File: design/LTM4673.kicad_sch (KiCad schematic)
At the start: 96 parts, among them U35 LTM4673IY#PBF

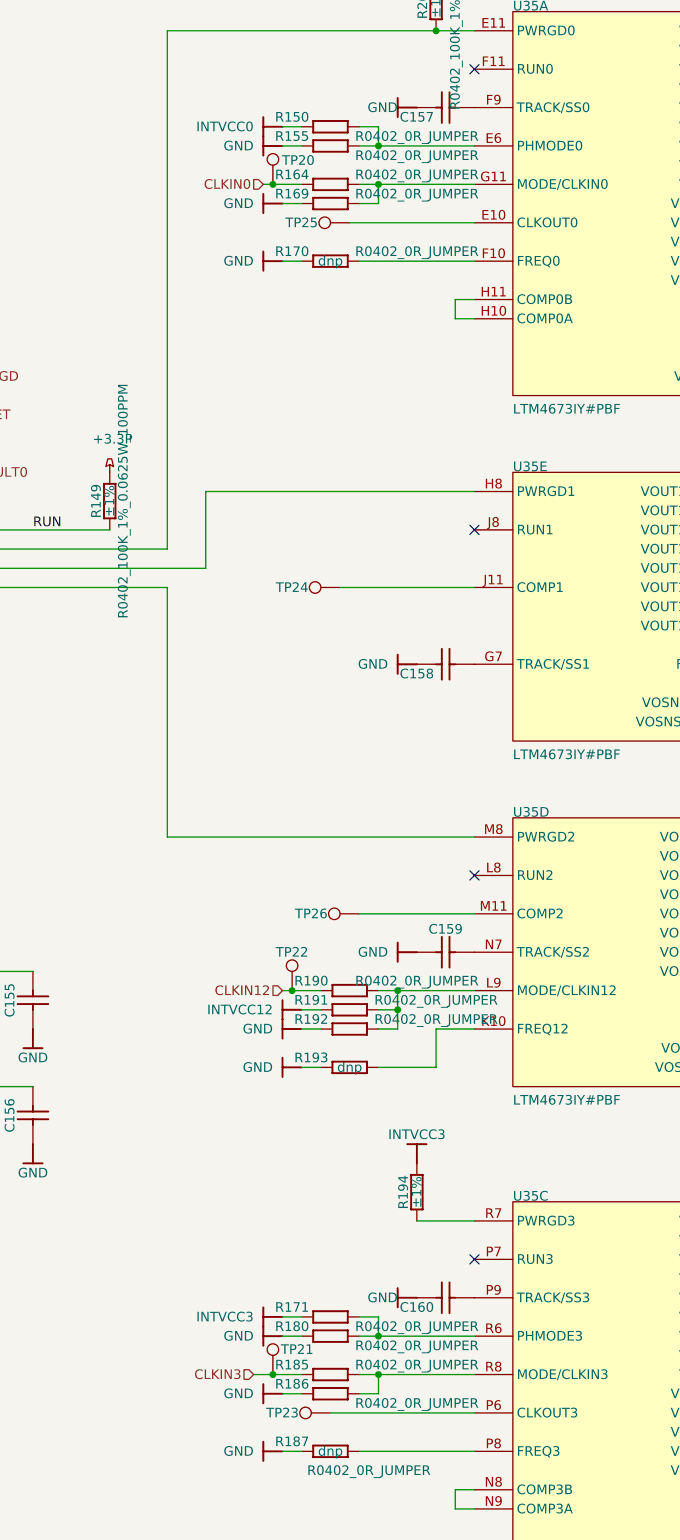
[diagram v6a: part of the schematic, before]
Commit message: some resistors marked as DNP
some resistors marked as DNP
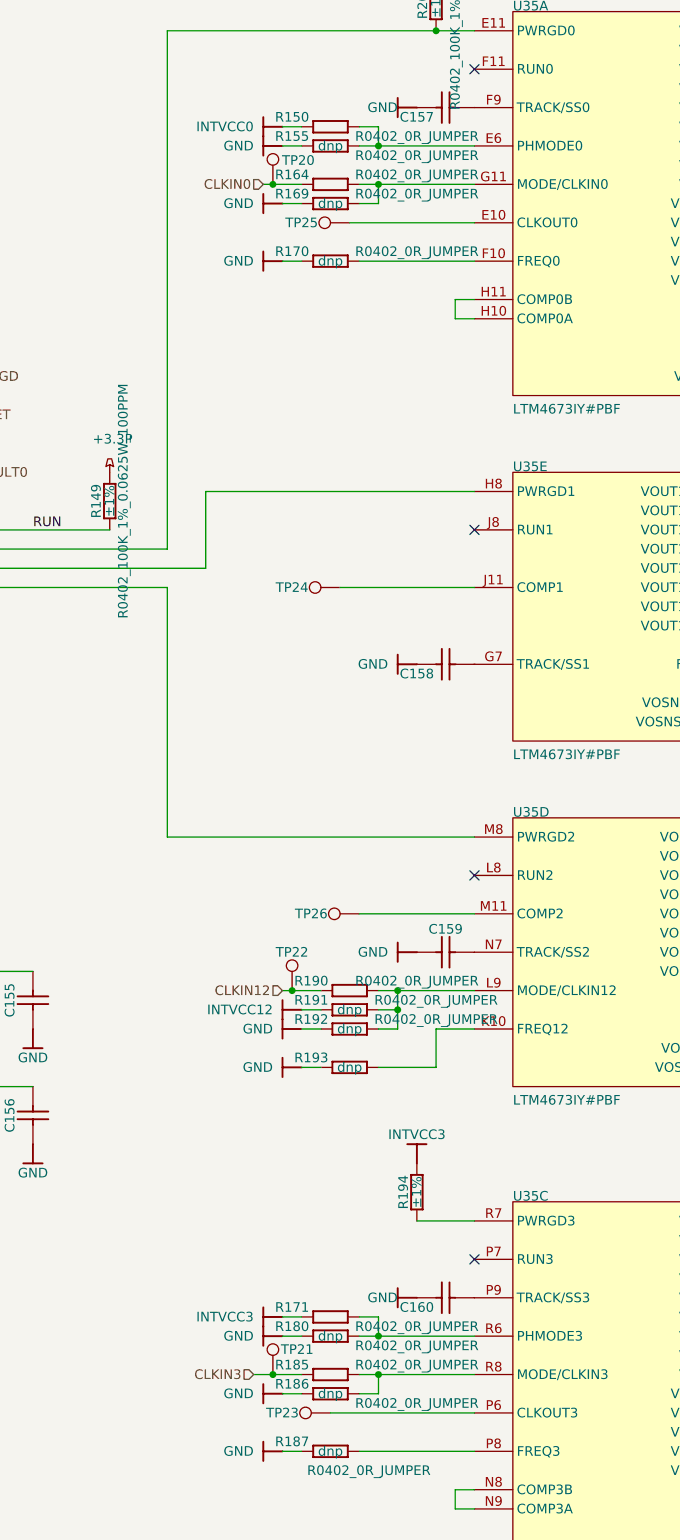
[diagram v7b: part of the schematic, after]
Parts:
- R105, R106, R140, R141, R143, R145, R148, R150, R164, R170, R171, R185, R187, R190, R193, R207, R208, R211, R218, R243, R244, R306, R307: Val (none) -> 0
- R155, R169, R180, R186, R191, R192: Val (none) -> 0; config (none) -> dnp
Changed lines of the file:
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@@
       (effects (font (size 1.27 1.27)) hide)
     )
+    (property "Val" "0" (id 28) (at 158.75 50.8 0)
+      (effects (font (size 1.27 1.27)) hide)
+    )
     (pin "1")
     (pin "2")
@@
       (effects (font (size 1.27 1.27)) hide)
     )
+    (property "Val" "0" (id 28) (at 100.33 104.14 0)
+      (effects (font (size 1.27 1.27)) hide)
+    )
     (pin "1")
     (pin "2")
@@
       (effects (font (size 1.27 1.27)) hide)
     )
+    (property "config" "dnp" (id 24) (at 162.56 218.44 0))
+    (property "Val" "0" (id 28) (at 158.75 218.44 0)
+      (effects (font (size 1.27 1.27)) hide)
+    )
     (pin "1")
     (pin "2")
@@
       (effects (font (size 1.27 1.27)) hide)
     )
+    (property "Val" "0" (id 28) (at 158.75 58.42 0)
+      (effects (font (size 1.27 1.27)) hide)
+    )
     (pin "1")
     (pin "2")
@@
       (effects (font (size 1.27 1.27)) hide)
     )
+    (property "Val" "0" (id 28) (at 257.81 210.82 0)
+      (effects (font (size 1.27 1.27)) hide)
+    )
     (pin "1")
     (pin "2")
@@
       (effects (font (size 1.27 1.27)) hide)
     )
+    (property "Val" "0" (id 28) (at 242.57 114.3 0)
+      (effects (font (size 1.27 1.27)) hide)
+    )
     (pin "1")
     (pin "2")
@@
     )
     (property "config" "dnp" (id 28) (at 165.1 175.26 0))
+    (property "Val" "0" (id 29) (at 161.29 175.26 0)
+      (effects (font (size 1.27 1.27)) hide)
+    )
     (pin "1")
     (pin "2")
@@
       (effects (font (size 1.27 1.27)) hide)
     )
+    (property "Val" "0" (id 28) (at 100.33 111.76 0)
+      (effects (font (size 1.27 1.27)) hide)
+    )
     (pin "1")
     (pin "2")
@@
       (effects (font (size 1.27 1.27)) hide)
     )
+    (property "Val" "0" (id 28) (at 161.29 165.1 0)
+      (effects (font (size 1.27 1.27)) hide)
+    )
     (pin "1")
     (pin "2")
@@
       (effects (font (size 1.27 1.27)) hide)
     )
+    (property "Val" "0" (id 28) (at 242.57 160.02 0)
+      (effects (font (size 1.27 1.27)) hide)
+    )
     (pin "1")
     (pin "2")
@@
       (effects (font (size 1.27 1.27)) hide)
     )
+    (property "Val" "0" (id 28) (at 158.75 208.28 0)
+      (effects (font (size 1.27 1.27)) hide)
+    )
     (pin "1")
     (pin "2")
@@
       (effects (font (size 1.27 1.27)) hide)
     )
+    (property "Val" "0" (id 28) (at 100.33 109.22 0)
+      (effects (font (size 1.27 1.27)) hide)
+    )
     (pin "1")
     (pin "2")
@@
       (effects (font (size 1.27 1.27)) hide)
     )
+    (property "Val" "0" (id 29) (at 158.75 68.58 0)
+      (effects (font (size 1.27 1.27)) hide)
+    )
     (pin "1")
     (pin "2")
@@
       (effects (font (size 1.27 1.27)) hide)
     )
+    (property "Val" "0" (id 28) (at 245.11 210.82 0)
+      (effects (font (size 1.27 1.27)) hide)
+    )
     (pin "1")
     (pin "2")
@@
       (effects (font (size 1.27 1.27)) hide)
     )
+    (property "config" "dnp" (id 24) (at 162.56 210.82 0))
+    (property "Val" "0" (id 28) (at 158.75 210.82 0)
+      (effects (font (size 1.27 1.27)) hide)
+    )
     (pin "1")
     (pin "2")
@@
       (effects (font (size 1.27 1.27)) hide)
     )
+    (property "config" "dnp" (id 24) (at 165.1 170.18 0))
+    (property "Val" "0" (id 28) (at 161.29 170.18 0)
+      (effects (font (size 1.27 1.27)) hide)
+    )
     (pin "1")
     (pin "2")
@@
       (effects (font (size 1.27 1.27)) hide)
     )
+    (property "Val" "0" (id 28) (at 257.81 106.68 0)
+      (effects (font (size 1.27 1.27)) hide)
+    )
     (pin "1")
     (pin "2")
@@
       (effects (font (size 1.27 1.27)) hide)
     )
+    (property "Val" "0" (id 28) (at 100.33 96.52 0)
+      (effects (font (size 1.27 1.27)) hide)
+    )
     (pin "1")
     (pin "2")
@@
       (effects (font (size 1.27 1.27)) hide)
     )
+    (property "config" "dnp" (id 24) (at 165.1 167.64 0))
+    (property "Val" "0" (id 28) (at 161.29 167.64 0)
+      (effects (font (size 1.27 1.27)) hide)
+    )
     (pin "1")
     (pin "2")
@@
       (effects (font (size 1.27 1.27)) hide)
     )
+    (property "config" "dnp" (id 24) (at 162.56 53.34 0))
+    (property "Val" "0" (id 28) (at 158.75 53.34 0)
+      (effects (font (size 1.27 1.27)) hide)
+    )
     (pin "1")
     (pin "2")
@@
       (effects (font (size 1.27 1.27)) hide)
     )
+    (property "Val" "0" (id 28) (at 44.45 76.2 0)
+      (effects (font (size 1.27 1.27)) hide)
+    )
     (pin "1")
     (pin "2")
@@
       (effects (font (size 1.27 1.27)) hide)
     )
+    (property "Val" "0" (id 28) (at 100.33 106.68 0)
+      (effects (font (size 1.27 1.27)) hide)
+    )
     (pin "1")
     (pin "2")
@@
       (effects (font (size 1.27 1.27)) hide)
     )
+    (property "Val" "0" (id 28) (at 158.75 215.9 0)
+      (effects (font (size 1.27 1.27)) hide)
+    )
     (pin "1")
     (pin "2")
@@
       (effects (font (size 1.27 1.27)) hide)
     )
+    (property "Val" "0" (id 28) (at 44.45 66.04 0)
+      (effects (font (size 1.27 1.27)) hide)
+    )
     (pin "1")
     (pin "2")
@@
       (effects (font (size 1.27 1.27)) hide)
     )
+    (property "Val" "0" (id 28) (at 245.11 53.34 0)
+      (effects (font (size 1.27 1.27)) hide)
+    )
     (pin "1")
     (pin "2")
@@
       (effects (font (size 1.27 1.27)) hide)
     )
+    (property "config" "dnp" (id 24) (at 162.56 60.96 0))
+    (property "Val" "0" (id 28) (at 158.75 60.96 0)
+      (effects (font (size 1.27 1.27)) hide)
+    )
     (pin "1")
     (pin "2")
@@
       (effects (font (size 1.27 1.27)) hide)
     )
+    (property "Val" "0" (id 28) (at 257.81 53.34 0)
+      (effects (font (size 1.27 1.27)) hide)
+    )
     (pin "1")
     (pin "2")
@@
       (effects (font (size 1.27 1.27)) hide)
     )
+    (property "Val" "0" (id 28) (at 257.81 152.4 0)
+      (effects (font (size 1.27 1.27)) hide)
+    )
     (pin "1")
     (pin "2")
@@
     )
     (property "config" "dnp" (id 28) (at 162.56 226.06 0))
+    (property "Val" "0" (id 29) (at 158.75 226.06 0)
+      (effects (font (size 1.27 1.27)) hide)
+    )
     (pin "1")
     (pin "2")

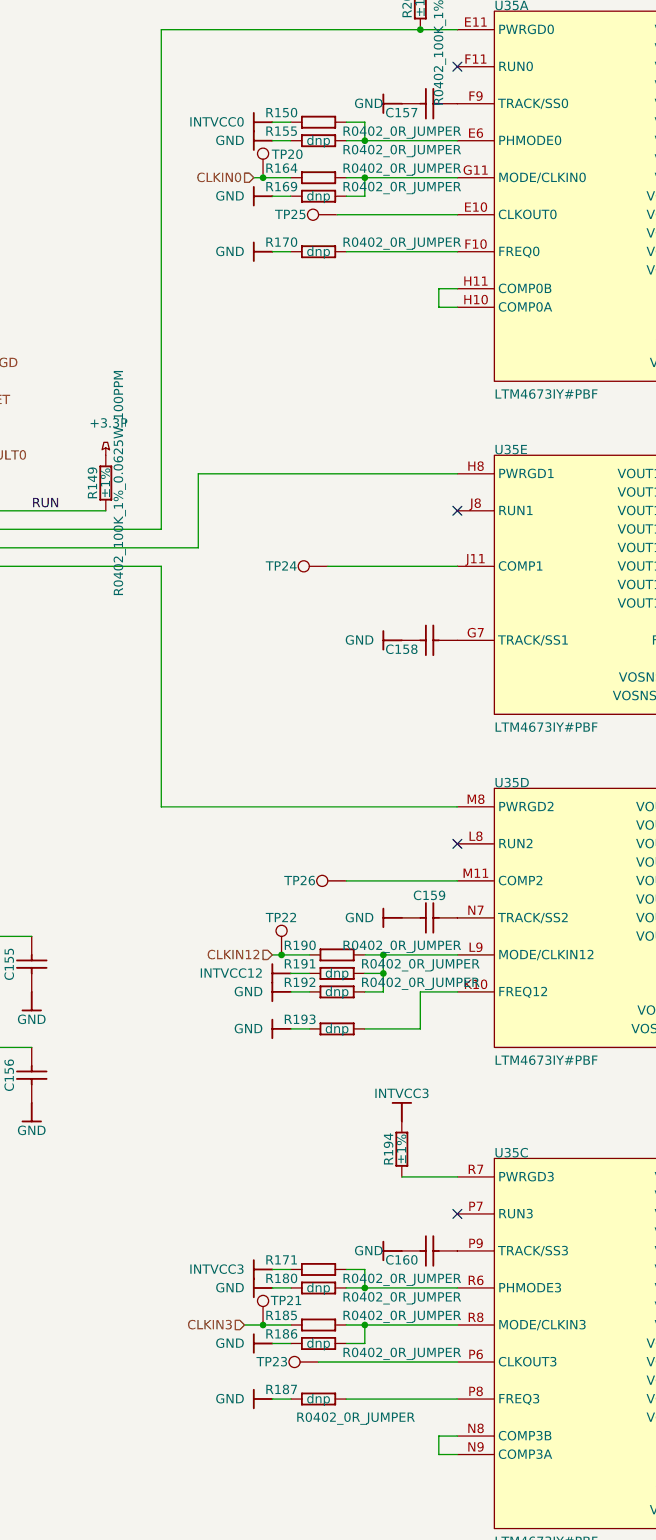
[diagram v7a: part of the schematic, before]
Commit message: Attempt to keep everything uniform by changing dnp to dnf. Also include thru parts in marble-xy.pos file
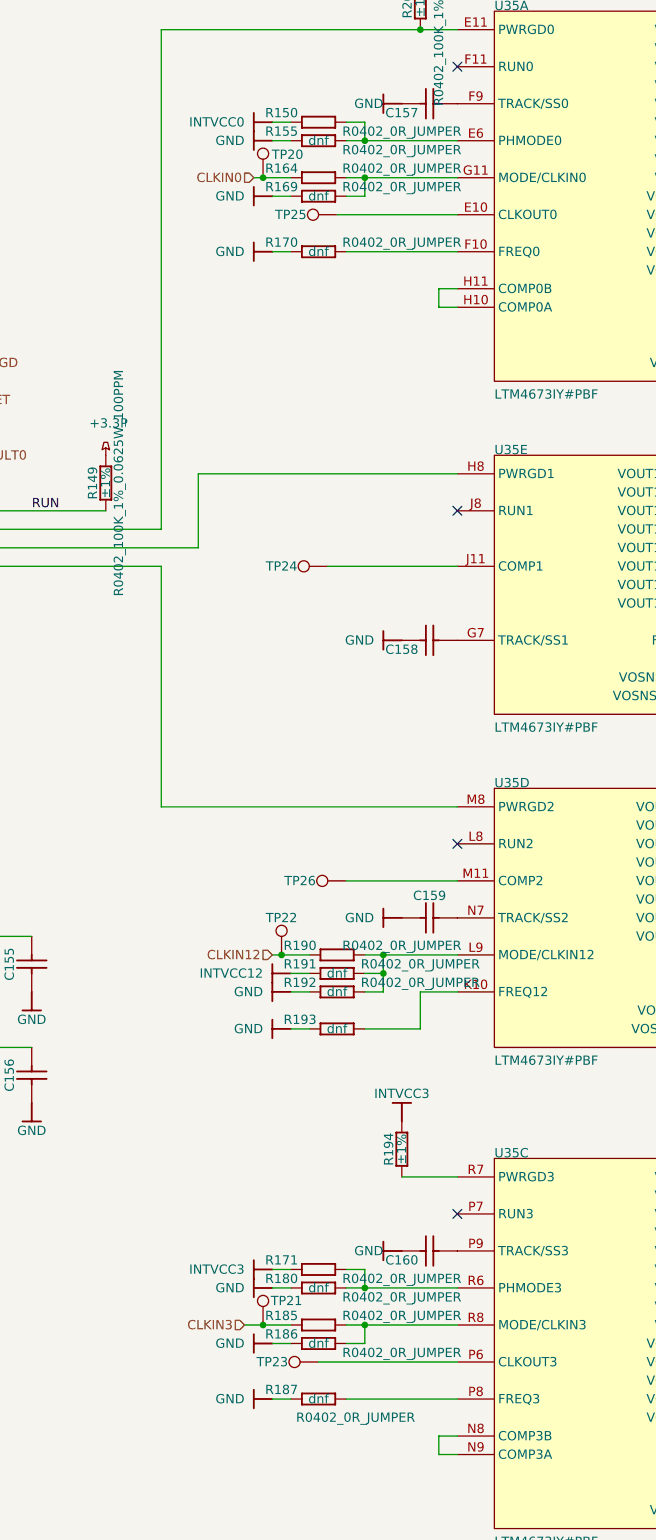
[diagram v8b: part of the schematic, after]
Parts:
- R155, R169, R170, R180, R186, R187, R191, R192, R193: config dnp -> dnf
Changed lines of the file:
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@@
       (effects (font (size 1.27 1.27)) hide)
     )
-    (property "config" "dnp" (id 24) (at 162.56 218.44 0))
+    (property "config" "dnf" (id 28) (at 162.56 218.44 0))
     (property "Val" "0" (id 28) (at 158.75 218.44 0)
       (effects (font (size 1.27 1.27)) hide)
@@
       (effects (font (size 1.27 1.27)) hide)
     )
-    (property "config" "dnp" (id 28) (at 165.1 175.26 0))
+    (property "config" "dnf" (id 28) (at 165.1 175.26 0))
     (property "Val" "0" (id 29) (at 161.29 175.26 0)
       (effects (font (size 1.27 1.27)) hide)
@@
       (effects (font (size 1.27 1.27)) (justify left bottom) hide)
     )
-    (property "config" "dnp" (id 27) (at 162.56 68.58 0))
+    (property "config" "dnf" (id 27) (at 162.56 68.58 0))
     (property "Manufacturer Part Number" "R0402_0R_JUMPER" (id 28) (at 158.75 68.58 0)
       (effects (font (size 1.27 1.27)) hide)
@@
       (effects (font (size 1.27 1.27)) hide)
     )
-    (property "config" "dnp" (id 24) (at 162.56 210.82 0))
+    (property "config" "dnf" (id 28) (at 162.56 210.82 0))
     (property "Val" "0" (id 28) (at 158.75 210.82 0)
       (effects (font (size 1.27 1.27)) hide)
@@
       (effects (font (size 1.27 1.27)) hide)
     )
-    (property "config" "dnp" (id 24) (at 165.1 170.18 0))
+    (property "config" "dnf" (id 28) (at 165.1 170.18 0))
     (property "Val" "0" (id 28) (at 161.29 170.18 0)
       (effects (font (size 1.27 1.27)) hide)
@@
       (effects (font (size 1.27 1.27)) hide)
     )
-    (property "config" "dnp" (id 24) (at 165.1 167.64 0))
+    (property "config" "dnf" (id 28) (at 165.1 167.64 0))
     (property "Val" "0" (id 28) (at 161.29 167.64 0)
       (effects (font (size 1.27 1.27)) hide)
@@
       (effects (font (size 1.27 1.27)) hide)
     )
-    (property "config" "dnp" (id 24) (at 162.56 53.34 0))
+    (property "config" "dnf" (id 28) (at 162.56 53.34 0))
     (property "Val" "0" (id 28) (at 158.75 53.34 0)
       (effects (font (size 1.27 1.27)) hide)
@@
       (effects (font (size 1.27 1.27)) hide)
     )
-    (property "config" "dnp" (id 24) (at 162.56 60.96 0))
+    (property "config" "dnf" (id 28) (at 162.56 60.96 0))
     (property "Val" "0" (id 28) (at 158.75 60.96 0)
       (effects (font (size 1.27 1.27)) hide)
@@
       (effects (font (size 1.27 1.27)) hide)
     )
-    (property "config" "dnp" (id 28) (at 162.56 226.06 0))
+    (property "config" "dnf" (id 28) (at 162.56 226.06 0))
     (property "Val" "0" (id 29) (at 158.75 226.06 0)
       (effects (font (size 1.27 1.27)) hide)
